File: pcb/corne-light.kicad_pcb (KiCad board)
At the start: 2 copper layers, 275.5 x 105.6 mm, 173 parts, among them J1 MJ-4PP-9, J2 OLED, J3 Conn_01x05, J5 Breakaway_Tabs, J6 MJ-4PP-9, J7 OLED, Q1 2N7002E, Q2 2N7002E, SW1 Rotary_Encoder_Switch, SW40 Rotary_Encoder_Switch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

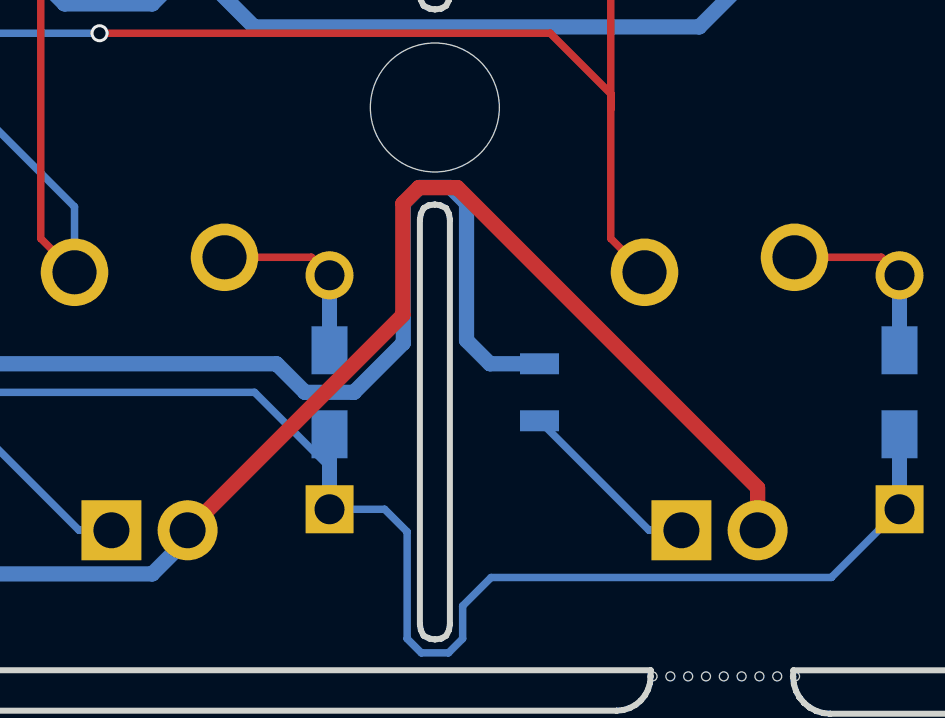
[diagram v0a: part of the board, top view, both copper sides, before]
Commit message: Fix vcc trace
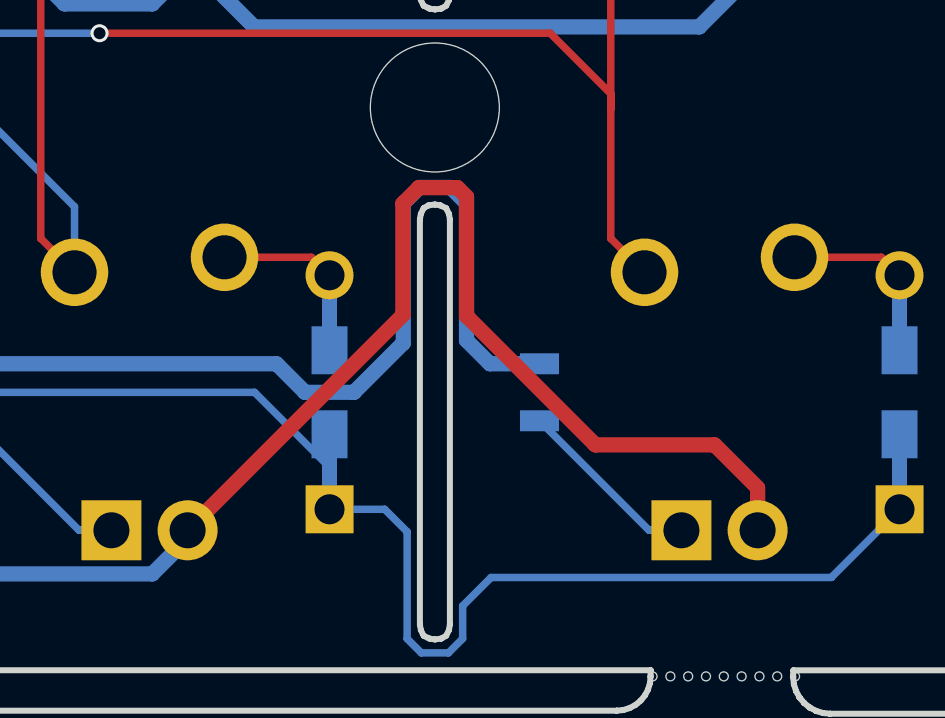
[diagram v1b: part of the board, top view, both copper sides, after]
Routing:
- net VDD: track 536.3 -> 538.7 mm

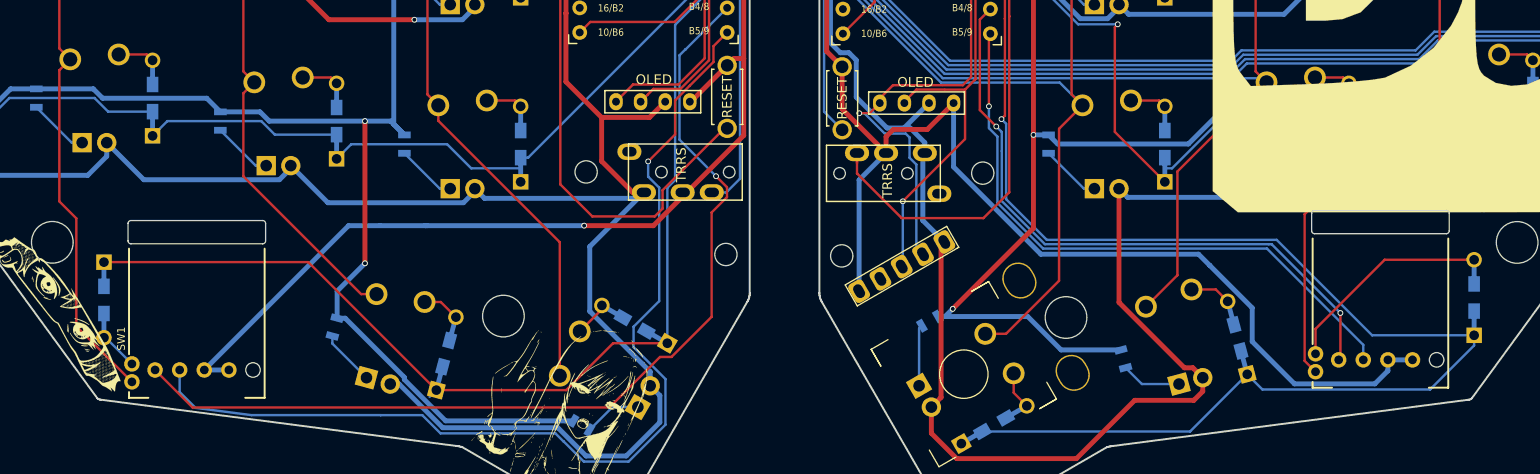
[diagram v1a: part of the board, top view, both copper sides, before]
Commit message: Fix DRC errors and rotate encoders
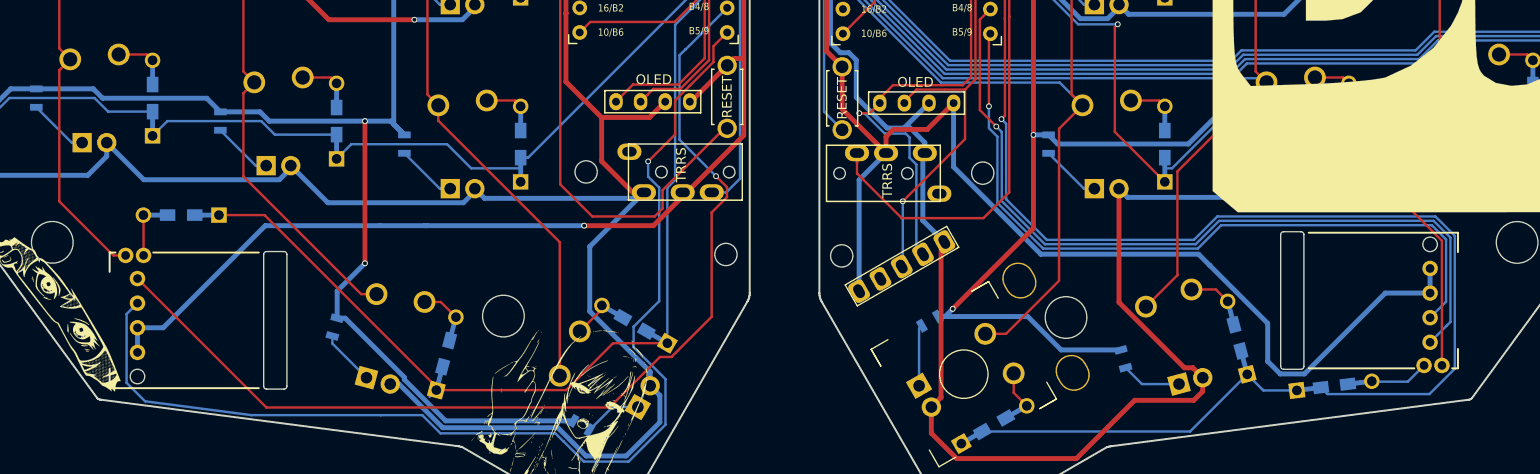
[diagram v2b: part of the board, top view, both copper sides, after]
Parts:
- moved D61 17.1 mm to (207.2, 106.5), turned to 187 degrees
- moved D13 11.8 mm to (88.1, 88.9), turned to 0 degrees
- turned SW1 to 0 degrees
- turned SW40 to 180 degrees
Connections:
- SW1 pad D: (no net) -> GND
- SW40 pad D: (no net) -> GNDA
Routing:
- net col3_r: track 150.9 -> 172.4 mm
- net ENCA_r: track 65.9 -> 82.8 mm, vias 2 -> 1
- net Net-(D61-Pad2): track 21.9 -> 7.52 mm
- net ENCB_r: track 63.8 -> 77.1 mm
- net col3: track 134.3 -> 121.7 mm
- net ENCB: track 103.5 -> 115.6 mm
- net row3: track 107.0 -> 97.3 mm
- net GNDA: track 162.7 -> 168.7 mm
- net ENCA: track 99.6 -> 105.3 mm
- net GND: track 131.6 -> 136.7 mm
- net row3_r: track 134.1 -> 137.5 mm
